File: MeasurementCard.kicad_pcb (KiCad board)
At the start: 2 copper layers, 218 parts, among them J1 Conn_01x05, J10 Conn_01x01, J13 Conn_01x01, J14 Conn_01x01, J17 Conn_01x03, J18 Conn_01x02, J2 Conn_01x02, J3 Conn_01x13, J4 Conn_01x03, J5 Conn_01x03, J6 Conn_01x03, J7 Conn_01x03, J8 Conn_01x13, J9 Conn_01x01, Q1 BSS138, Q10 BSS138, Q11 BSS138, Q12 BSS138, Q13 NSV1C201MZ4, Q14 BSS138, Q15 BSS138, Q16 BSS138, Q17 BSS138, Q18 BSS138, Q19 BSS138, Q2 BSS138, Q20 BSS138, Q21 BSS138, Q22 BSS138, Q23 BSS138, Q24 BSS138, Q25 BSS138, Q26 NSV1C201MZ4, Q3 BSS138, Q4 BSS138, Q5 BSS138, Q6 BSS138, Q7 BSS138, Q8 BSS138, Q9 BSS138, T1 HX1188NL, T2 HX1188NL, U1 LTC6804-1, U2 LTC6804-1

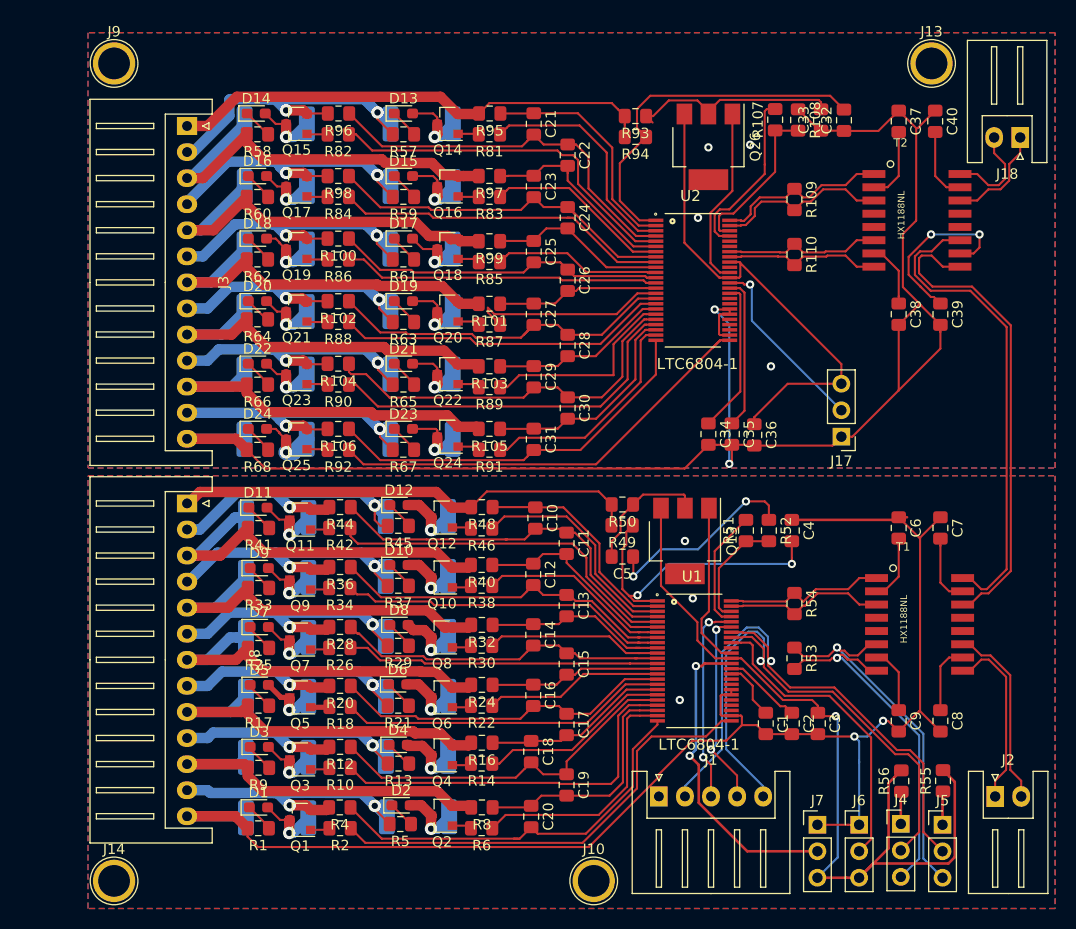
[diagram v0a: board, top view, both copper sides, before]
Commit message: added db25 + thermistor support
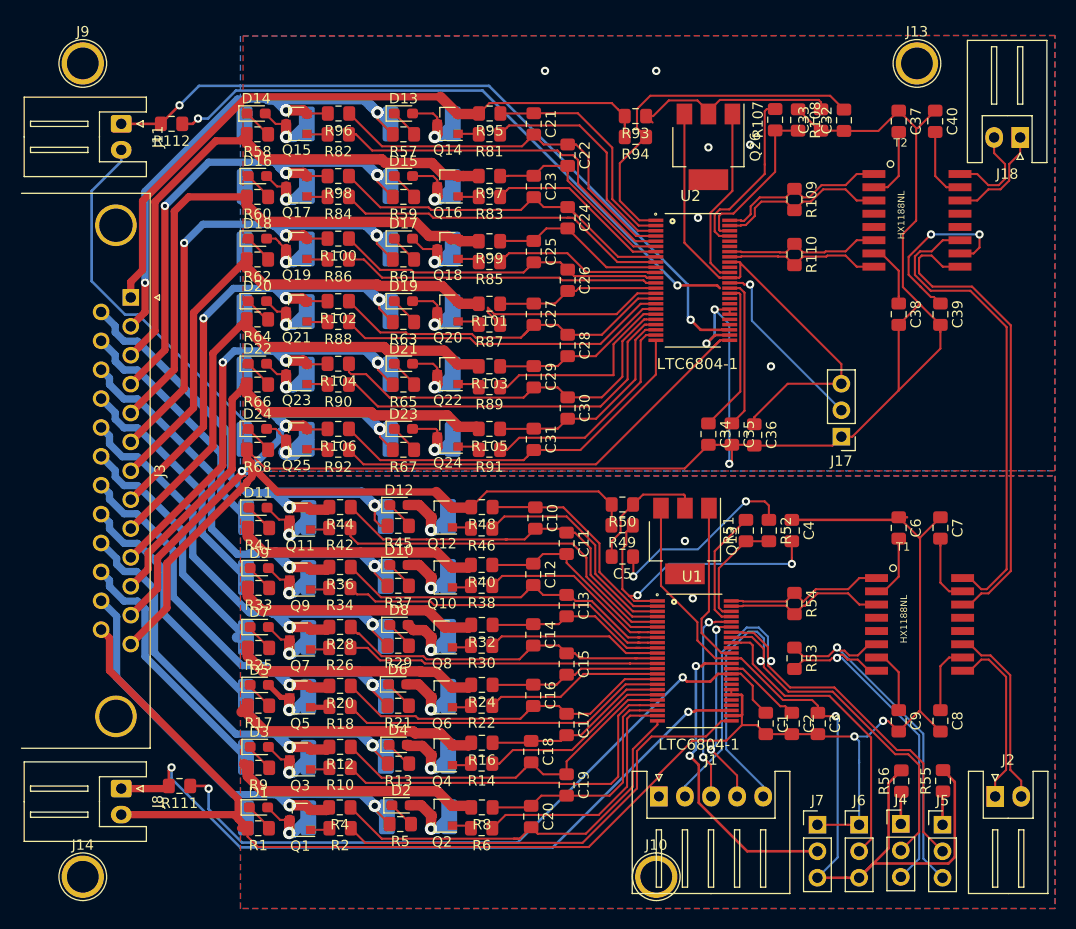
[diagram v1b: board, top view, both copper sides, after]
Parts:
- added J11: Conn_01x02, Connector_JST:JST_XH_S2B-XH-A_1x02_P2.50mm_Horizontal, F.Cu at (43.7, 79.0)
- added R111: 10k, Resistor_SMD:R_0805_2012Metric_Pad1.15x1.40mm_HandSolder, F.Cu at (49.3, 142.5)
- added R112: 10k, Resistor_SMD:R_0805_2012Metric_Pad1.15x1.40mm_HandSolder, F.Cu at (48.5, 79.0)
- J3: value Conn_01x13 -> Conn_01x25; footprint Connector_JST:JST_XH_S13B-XH-A_1x13_P2.50mm_Horizontal -> Connector_Dsub:DSUB-25_Male_Horizontal_P2.77x2.84mm_EdgePinOffset7.70mm_Housed_MountingHolesOffset9.12mm
- J8: value Conn_01x13 -> Conn_01x02; footprint Connector_JST:JST_XH_S13B-XH-A_1x13_P2.50mm_Horizontal -> Connector_JST:JST_XH_S2B-XH-A_1x02_P2.50mm_Horizontal
- moved J8 28.1 mm to (43.7, 142.7)
- moved J3 17.3 mm to (44.6, 95.6)
- moved J10 6.01 mm to (95.0, 151.2)
- moved J14 3.03 mm to (40.0, 151.2)
- moved J9 3.00 mm to (40.0, 73.2)
- moved J13 1.40 mm to (120.0, 73.2)
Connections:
- net Net-(C1-Pad1) renamed VREF2_1
- net Net-(C35-Pad1) renamed VREF2_2
- J8 pad 1: Net-(J8-Pad1) -> VTEMP1
- J8 pad 2: Net-(J8-Pad2) -> GND
- Q1 pad 2: Net-(J8-Pad12) -> Net-(J3-Pad24)
- Q10 pad 2: Net-(J8-Pad3) -> Net-(J3-Pad15)
- Q11 pad 2: Net-(J8-Pad2) -> Net-(J3-Pad14)
- Q12 pad 2: Net-(J8-Pad1) -> GNDA
- Q2 pad 2: Net-(J8-Pad11) -> Net-(J3-Pad23)
- Q3 pad 2: Net-(J8-Pad10) -> Net-(J3-Pad22)
- Q4 pad 2: Net-(J8-Pad9) -> Net-(J3-Pad21)
- Q5 pad 2: Net-(J8-Pad8) -> Net-(J3-Pad20)
- Q6 pad 2: Net-(J8-Pad7) -> Net-(J3-Pad19)
- Q7 pad 2: Net-(J8-Pad6) -> Net-(J3-Pad18)
- Q8 pad 2: Net-(J8-Pad5) -> Net-(J3-Pad17)
- Q9 pad 2: Net-(J8-Pad4) -> Net-(J3-Pad16)
- R11 pad 1: Net-(J8-Pad11) -> Net-(J3-Pad23)
- R12 pad 2: Net-(J8-Pad10) -> Net-(J3-Pad22)
- R13 pad 2: Net-(J8-Pad10) -> Net-(J3-Pad22)
- R15 pad 1: Net-(J8-Pad10) -> Net-(J3-Pad22)
- R16 pad 2: Net-(J8-Pad9) -> Net-(J3-Pad21)
- R17 pad 2: Net-(J8-Pad9) -> Net-(J3-Pad21)
- R19 pad 1: Net-(J8-Pad9) -> Net-(J3-Pad21)
- R20 pad 2: Net-(J8-Pad8) -> Net-(J3-Pad20)
- R21 pad 2: Net-(J8-Pad8) -> Net-(J3-Pad20)
- R23 pad 1: Net-(J8-Pad8) -> Net-(J3-Pad20)
- R24 pad 2: Net-(J8-Pad7) -> Net-(J3-Pad19)
- R25 pad 2: Net-(J8-Pad7) -> Net-(J3-Pad19)
- R27 pad 1: Net-(J8-Pad7) -> Net-(J3-Pad19)
- R28 pad 2: Net-(J8-Pad6) -> Net-(J3-Pad18)
- R29 pad 2: Net-(J8-Pad6) -> Net-(J3-Pad18)
- R31 pad 1: Net-(J8-Pad6) -> Net-(J3-Pad18)
- R32 pad 2: Net-(J8-Pad5) -> Net-(J3-Pad17)
- R33 pad 2: Net-(J8-Pad5) -> Net-(J3-Pad17)
- R35 pad 1: Net-(J8-Pad5) -> Net-(J3-Pad17)
- R36 pad 2: Net-(J8-Pad4) -> Net-(J3-Pad16)
- R37 pad 2: Net-(J8-Pad4) -> Net-(J3-Pad16)
- R39 pad 1: Net-(J8-Pad4) -> Net-(J3-Pad16)
- R4 pad 2: Net-(J8-Pad12) -> Net-(J3-Pad24)
- R40 pad 2: Net-(J8-Pad3) -> Net-(J3-Pad15)
- R41 pad 2: Net-(J8-Pad3) -> Net-(J3-Pad15)
- R43 pad 1: Net-(J8-Pad3) -> Net-(J3-Pad15)
- R44 pad 2: Net-(J8-Pad2) -> Net-(J3-Pad14)
- R45 pad 2: Net-(J8-Pad2) -> Net-(J3-Pad14)
- R47 pad 1: Net-(J8-Pad2) -> Net-(J3-Pad14)
- R48 pad 2: Net-(J8-Pad1) -> GNDA
- R49 pad 2: Net-(J8-Pad1) -> GNDA
- R5 pad 2: Net-(J8-Pad12) -> Net-(J3-Pad24)
- R50 pad 2: Net-(J8-Pad1) -> GNDA
- R7 pad 1: Net-(J8-Pad12) -> Net-(J3-Pad24)
- R8 pad 2: Net-(J8-Pad11) -> Net-(J3-Pad23)
- R9 pad 2: Net-(J8-Pad11) -> Net-(J3-Pad23)
- U1 pad 27: Net-(U1-Pad27) -> VTEMP1
- U2 pad 27: Net-(U2-Pad27) -> VTEMP2
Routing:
- net GNDA: track 155.6 -> 245.6 mm, vias 6 -> 9
- net VTEMP2: track 0.00 -> 71.4 mm, vias 0 -> 2
- net VTEMP1: track 0.00 -> 69.5 mm, vias 0 -> 2
- net VREF2_1: track 5.67 -> 68.0 mm, vias 0 -> 2
- net VREF2_2: track 14.6 -> 75.4 mm, vias 0 -> 2
- net Net-(J3-Pad22): track 0.00 -> 48.7 mm, vias 0 -> 2
- net Net-(J3-Pad24): track 0.00 -> 48.6 mm, vias 0 -> 2
- net Net-(J3-Pad16): track 0.00 -> 48.4 mm, vias 0 -> 2
- net Net-(J3-Pad21): track 0.00 -> 48.4 mm
- net Net-(J3-Pad19): track 0.00 -> 48.3 mm
- net Net-(J3-Pad23): track 0.00 -> 48.3 mm
- net Net-(J3-Pad18): track 0.00 -> 47.6 mm, vias 0 -> 2
- net Net-(J3-Pad17): track 0.00 -> 47.2 mm
- net Net-(J3-Pad20): track 0.00 -> 47.0 mm, vias 0 -> 2
- net Net-(J3-Pad15): track 0.00 -> 47.0 mm
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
